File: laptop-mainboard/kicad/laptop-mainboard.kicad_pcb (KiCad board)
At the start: 8 copper layers, 330 x 115 mm, 112 parts, among them Q1 SiSS22DN, Q2 SiSS22DN, Q3 SiSS22DN, Q4 SiSS22DN, Q5 BATFET, U1 TPS65988 PD, U11 MP2857, U12 Stage CPU1, U13 Stage CPU2, U14 Stage CPU3, U15 Stage CPU4, U16 Stage SOC1, U17 Stage SOC2, U18 1V1_MEM, U19 W25Q256JW, U2 PD-Cfg, U21 SSD1-SW, U22 SSD2-SW, U23 JHL8540 TB4, U28 HD3SS3220, U29 HD3SS3220, U3 BQ25731, U30 VBUS-SW, U31 VBUS-SW, U32 VBUS-SW, U33 VBUS-SW, U34 RTL8125BG, U35 RTL8125BG, U36 TPD12S016, U37 VLCD-SW, U38 MP3389 BL, U39 ALC256, U4 5V Buck, U40 GL3224 SD, U41 IT5570E EC, U42 EC-Flash, U5 3V3 Buck, U6 1V8, U7 1V05_TB, U8 0V88_TB, U9 3V3_ALW, Y1 32.768k, Y3 25M, Y4 25M

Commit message: Rev B: echte AM5-Pinbelegung, Kleinteile, EliteBook-850-G7-Format
- AM5-Pinmap (1718 Pins, WikiChip/Wikimedia Public Domain) als CSV,
  Sockel-Footprint mit echten Padnamen und 1708 Signal-Netzen im Board
- Blatt 10: MLCC-Baenke, 11 ESD-Arrays, USB2-Chokes, Straps; 48-MHz-Quarz;
  beidseitige Bestueckung (B.Cu) mit Kollisionspruefung pro Seite
- Board 340x112mm im EliteBook-850-G7-Layout: USB-C-100W-PD an der
  Barrel-Jack-Position, TB4/HDMI/USB-A/RJ45 rechts, USB-A/Klinke links,
  HP-Akku 3S/56Wh, HP-FPC-Steckplaetze (Pinouts zu verifizieren)
- GND-Stitching-Vias, MDI-/DP-Korridore, 645 Board-Netze
- Renderer tools/render_board.py erzeugt docs/board_render.png
- Doku: elitebook.md neu, grenzen.md/README/power/layout aktualisiert

Co-Authored-By: Claude Fable 5 <noreply@anthropic.com>
Claude-Session: https://claude.ai/code/session_01E8mU1RUAv938Hs69waADCc
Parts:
- removed C14: 1n/2kV, laptop_mainboard:C_1812
- removed the C5 at (104.0, 122.0)
- removed J_LAN2: 2.5GbE, laptop_mainboard:RJ45_MAGJACK
- removed J_SD: SD UHS-II, laptop_mainboard:SD_PUSH
- removed J_USBC2, J_USBC3: USB-C 10G, laptop_mainboard:USBC_24
- removed U28, U29: HD3SS3220, laptop_mainboard:QFN30_4x4
- removed U30, U31: VBUS-SW, laptop_mainboard:SOT23-5
- removed U35: RTL8125BG, laptop_mainboard:QFN48_6x6
- removed U40: GL3224 SD, laptop_mainboard:QFN48_6x6
- removed Y4: 25M, laptop_mainboard:XTAL_3225
- added C20: 22u, laptop_mainboard:R_0603, B.Cu at (112.0, 72.0)
- added C21: 22u, laptop_mainboard:R_0603, B.Cu at (122.0, 72.0)
- added C22: 22u, laptop_mainboard:R_0603, B.Cu at (132.0, 72.0)
- added C23: 22u, laptop_mainboard:R_0603, B.Cu at (142.0, 72.0)
- added C24: 22u, laptop_mainboard:R_0603, B.Cu at (112.0, 80.0)
- added C25: 22u, laptop_mainboard:R_0603, B.Cu at (122.0, 80.0)
- added C26: 22u, laptop_mainboard:R_0603, B.Cu at (132.0, 80.0)
- added C27: 22u, laptop_mainboard:R_0603, B.Cu at (142.0, 80.0)
- added C28: 22u, laptop_mainboard:R_0603, B.Cu at (112.0, 88.0)
- added C29: 22u, laptop_mainboard:R_0603, B.Cu at (122.0, 88.0)
- added C30: 22u, laptop_mainboard:R_0603, B.Cu at (132.0, 88.0)
- added C31: 22u, laptop_mainboard:R_0603, B.Cu at (142.0, 88.0)
- added C32: 22u, laptop_mainboard:R_0603, B.Cu at (104.0, 96.0)
- added C33: 22u, laptop_mainboard:R_0603, B.Cu at (114.0, 96.0)
- added C34: 22u, laptop_mainboard:R_0603, B.Cu at (124.0, 96.0)
- added C35: 22u, laptop_mainboard:R_0603, B.Cu at (104.0, 64.0)
- added C36: 22u, laptop_mainboard:R_0603, B.Cu at (114.0, 64.0)
- added C40: 10u, laptop_mainboard:R_0603, B.Cu at (170.0, 60.0)
- added C41: 10u, laptop_mainboard:R_0603, B.Cu at (178.0, 60.0)
- added C42: 10u, laptop_mainboard:R_0603, B.Cu at (186.0, 60.0)
- added C43: 10u, laptop_mainboard:R_0603, B.Cu at (194.0, 60.0)
- added C44: 10u, laptop_mainboard:R_0603, B.Cu at (202.0, 60.0)
- added C45: 10u, laptop_mainboard:R_0603, B.Cu at (210.0, 60.0)
- added C46: 10u, laptop_mainboard:R_0603, B.Cu at (218.0, 60.0)
- added C47: 10u, laptop_mainboard:R_0603, B.Cu at (226.0, 60.0)
- added C48: 10u, laptop_mainboard:R_0603, B.Cu at (234.0, 60.0)
- added C49: 10u, laptop_mainboard:R_0603, B.Cu at (242.0, 60.0)
- added C52: 100n, laptop_mainboard:R_0603, B.Cu at (170.0, 68.0)
- added C53: 100n, laptop_mainboard:R_0603, B.Cu at (178.0, 68.0)
- added C54: 100n, laptop_mainboard:R_0603, B.Cu at (186.0, 68.0)
- added C55: 100n, laptop_mainboard:R_0603, B.Cu at (194.0, 68.0)
- added C56: 100n, laptop_mainboard:R_0603, B.Cu at (202.0, 68.0)
- added C57: 100n, laptop_mainboard:R_0603, B.Cu at (210.0, 68.0)
- added C58: 100n, laptop_mainboard:R_0603, B.Cu at (218.0, 68.0)
- added C59: 100n, laptop_mainboard:R_0603, B.Cu at (226.0, 68.0)
- added C60: 100n, laptop_mainboard:R_0603, B.Cu at (234.0, 68.0)
- added C61: 100n, laptop_mainboard:R_0603, B.Cu at (242.0, 68.0)
- added FL1: CMC Webcam, laptop_mainboard:R_0603, B.Cu at (203.0, 40.0)
- added FL2: CMC WLAN, laptop_mainboard:R_0603, B.Cu at (292.0, 52.0)
- added H6: , laptop_mainboard:MTG_M2_5, F.Cu at (274.0, 80.0)
- added R10: 10k, laptop_mainboard:R_0603, B.Cu at (60.0, 40.0)
- added R11: 10k, laptop_mainboard:R_0603, B.Cu at (60.0, 46.0)
- added R12: 10k, laptop_mainboard:R_0603, B.Cu at (60.0, 52.0)
- added R13: 10k, laptop_mainboard:R_0603, B.Cu at (60.0, 58.0)
- added R14: 10k, laptop_mainboard:R_0603, B.Cu at (60.0, 64.0)
- added R15: 10k, laptop_mainboard:R_0603, B.Cu at (60.0, 70.0)
- added U5: 3V3 Buck, laptop_mainboard:QFN20_3x4, F.Cu at (109.0, 38.0)
- added U50: ESD TB0-L1, laptop_mainboard:DFN6_2x2, B.Cu at (344.0, 40.0)
- added U51: ESD TB0-L2, laptop_mainboard:DFN6_2x2, B.Cu at (344.0, 46.0)
- added U52: ESD TB1-L1, laptop_mainboard:DFN6_2x2, B.Cu at (344.0, 52.0)
- added U53: ESD TB1-L2, laptop_mainboard:DFN6_2x2, B.Cu at (344.0, 58.0)
- added U54: ESD USBA1, laptop_mainboard:DFN6_2x2, B.Cu at (46.0, 60.0)
- added U55: ESD USBA2, laptop_mainboard:DFN6_2x2, B.Cu at (344.0, 90.0)
- added U56: ESD HDMI-1, laptop_mainboard:DFN6_2x2, B.Cu at (342.0, 70.0)
- added U57: ESD HDMI-2, laptop_mainboard:DFN6_2x2, B.Cu at (342.0, 76.0)
- added U58: ESD CC, laptop_mainboard:DFN6_2x2, B.Cu at (350.0, 34.0)
- added U59: ESD TB-USB2, laptop_mainboard:DFN6_2x2, B.Cu at (344.0, 64.0)
- added U60: ESD A-USB2, laptop_mainboard:DFN6_2x2, B.Cu at (46.0, 68.0)
- added Y2: 48M, laptop_mainboard:XTAL_3225, F.Cu at (183.0, 48.0)
- C37: renamed from H6; value (none) -> 22u; footprint laptop_mainboard:MTG_M2_5 -> laptop_mainboard:R_0603; moved to B.Cu
- C5: renamed from U5; value 3V3 Buck -> 470u; footprint laptop_mainboard:QFN20_3x4 -> laptop_mainboard:CAP_7343
- J_BAT: value Akku 4S -> HP-Akku 3S 56Wh
- J_KB: value Tastatur -> HP-Tastatur
- J_TB0: value TB4 / 100W PD -> USB-C PD 100W + TB4
- J_TP: value Touchpad -> HP-Clickpad
- moved J_LAN1 316.9 mm to (352.0, 112.0), turned to 270 degrees
- moved J_USBA2 314.8 mm to (352.0, 90.0), turned to 270 degrees
- moved C13 274.2 mm to (330.0, 104.0)
- moved U34 273.1 mm to (325.0, 112.0)
- moved U33 264.7 mm to (330.0, 92.0)
- moved Y3 256.6 mm to (316.0, 118.0)
- moved C37 150.9 mm to (124.0, 64.0)
- moved C5 82.2 mm to (104.0, 120.0)
- moved BT1 51.0 mm to (223.0, 133.0), turned to 90 degrees
- moved J_SPKR 39.3 mm to (276.0, 131.0)
- moved J_USBA1 36.0 mm to (40.0, 60.0)
- moved U32 33.5 mm to (58.0, 60.0)
- moved J_AUX 30.0 mm to (38.0, 84.0)
- moved J_HDMI 26.0 mm to (350.0, 70.0)
- moved H7 19.6 mm to (28.0, 105.0)
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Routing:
- net (no net): track 3613.1 -> 4365.7 mm
- net GND: vias 0 -> 83
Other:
- board size 330 x 115 mm -> 340 x 112 mm
- board text added: "HP-Akkuschacht (3S 56Wh) unterhalb"
- board text added: "Laptop-Mainboard fuer HP EliteBook 850 G7 - Rev B"
- board text added: "Umriss + Lochbild am realen 850-G7-Chassis verifizieren (docs/elitebook.md)"
- board text removed: "Akku-Bereich unterhalb der Platine"
- board text removed: "Korridore In1/In6: DDR5- und PCIe-Gen4-Paare (repraesentativ, Feinrouting offen)"
- board text removed: "Laptop-Mainboard 15.6" Rev A"

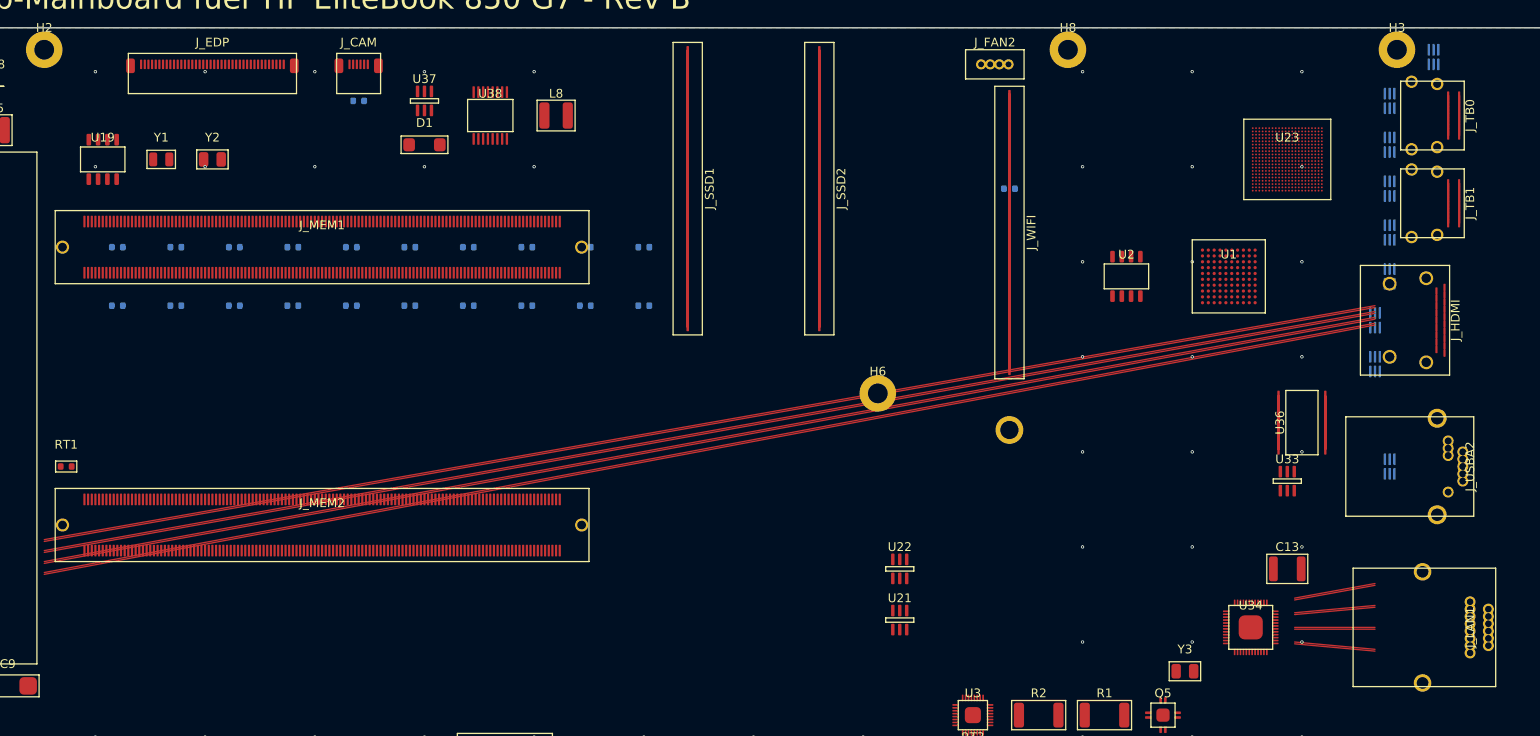
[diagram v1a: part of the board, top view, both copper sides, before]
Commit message: Portlayout nach Fotos des Originalgeraets korrigiert
- Rechte Kante hinten->vorn: USB-C-Ladeport 100W (Barrel-Position,
  eigener TPS65987D + Config-Flash, neues Blatt 07_ladeport), USB-A,
  HDMI, 2x USB-C Thunderbolt 4 nebeneinander (JHL8540)
- Kein RJ45 (Original hat keines): Ethernet entfernt, G0/G1 Reserve
- TPS65988 nur noch Source fuer die TB-Ports; breite VBUS_IN-Trasse
  vom Ladeport zum BQ25731
- Interne Anschlusspositionen des Original-Mainboards (Nutzerfoto)
  als Referenztabelle in docs/elitebook.md dokumentiert
- Doku, Blockdiagramm, BOM und Rendering aktualisiert

Co-Authored-By: Claude Fable 5 <noreply@anthropic.com>
Claude-Session: https://claude.ai/code/session_01E8mU1RUAv938Hs69waADCc
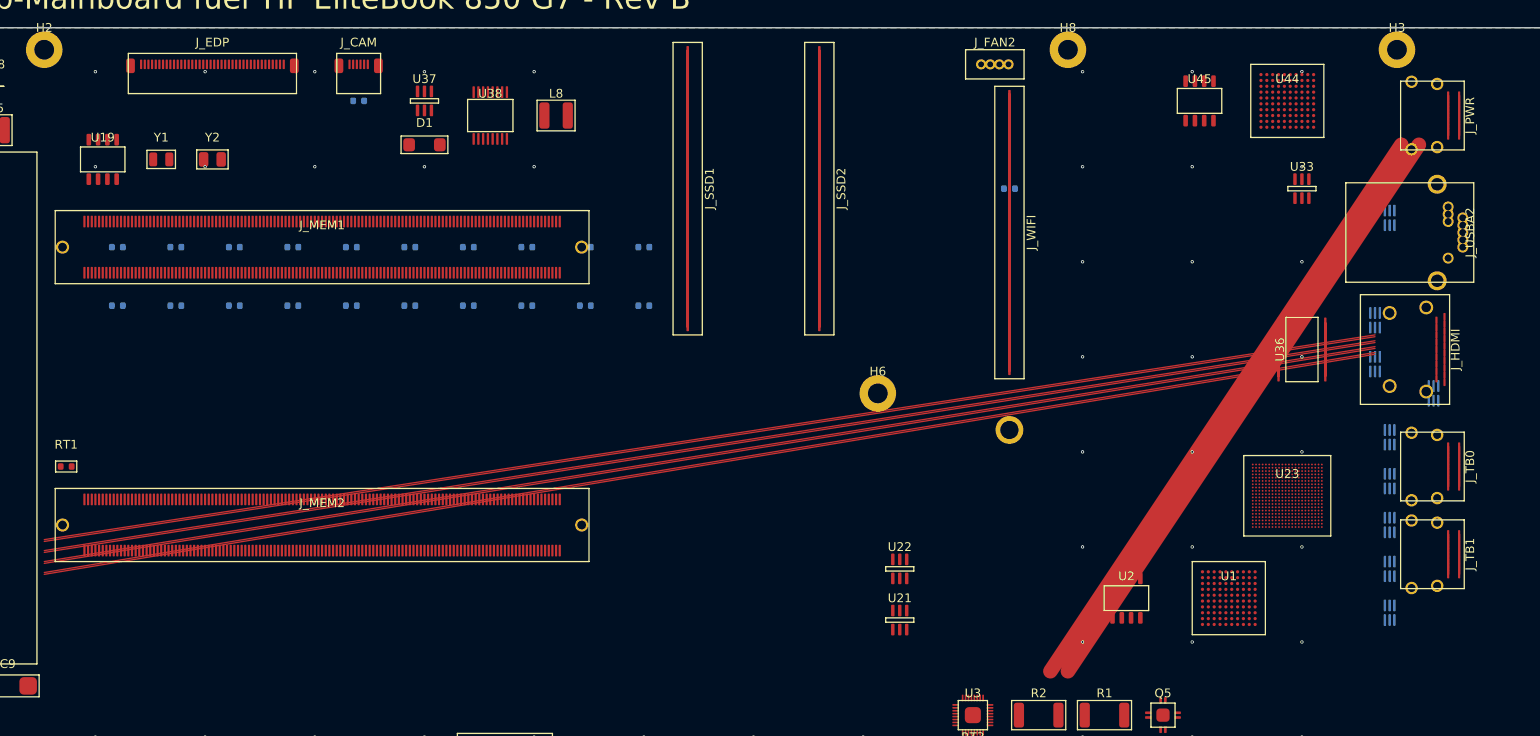
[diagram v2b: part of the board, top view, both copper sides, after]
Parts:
- removed C13: 1n/2kV, laptop_mainboard:C_1812
- removed the C20 at (112.0, 72.0)
- removed J_LAN1: 2.5GbE, laptop_mainboard:RJ45_MAGJACK
- removed the L10 at (109.0, 44.0)
- removed the U1 at (322.0, 64.0)
- removed U34: RTL8125BG, laptop_mainboard:QFN48_6x6
- removed the U6 at (129.0, 38.0)
- removed the U9 at (120.0, 38.0)
- removed Y3: 25M, laptop_mainboard:XTAL_3225
- added H1: , laptop_mainboard:MTG_M2_5, F.Cu at (28.0, 33.0)
- added J_PWR: USB-C Ladeport 100W, laptop_mainboard:USBC_24, F.Cu at (352.0, 42.0)
- added U36: TPD12S016, laptop_mainboard:TSSOP24, F.Cu at (332.0, 74.0)
- added U4: 5V Buck, laptop_mainboard:QFN20_3x4, F.Cu at (98.0, 38.0)
- added U44: TPS65987D Ladeport, laptop_mainboard:BGA96_9x9, F.Cu at (330.0, 40.0)
- added U45: PD2-Cfg, laptop_mainboard:SOIC8, F.Cu at (318.0, 40.0)
- added U5: 3V3 Buck, laptop_mainboard:QFN20_3x4, F.Cu at (109.0, 38.0)
- added U7: 1V05_TB, laptop_mainboard:DFN6_2x2, F.Cu at (137.0, 38.0)
- C20: renamed from H8; value (none) -> 22u; footprint laptop_mainboard:MTG_M2_5 -> laptop_mainboard:R_0603; moved to B.Cu
- J_TB0: value USB-C PD 100W + TB4 -> USB-C TB4
- J_TB1: value TB4 -> USB-C TB4
- L10: renamed from U7; value 1V05_TB -> 1u; footprint laptop_mainboard:DFN6_2x2 -> laptop_mainboard:IND_4x4
- U1: renamed from U36; value TPD12S016 -> TPS65988 PD; footprint laptop_mainboard:TSSOP24 -> laptop_mainboard:BGA96_9x9
- U6: renamed from U5; value 3V3 Buck -> 1V8; footprint laptop_mainboard:QFN20_3x4 -> laptop_mainboard:DFN6_2x2
- U9: renamed from U4; value 5V Buck -> 3V3_ALW
- moved H4 332.0 mm to (30.0, 138.0)
- moved H8 281.4 mm to (300.0, 33.0)
- moved H7 247.3 mm to (28.0, 105.0)
- moved H5 210.0 mm to (240.0, 139.0)
- moved C20 192.0 mm to (112.0, 72.0)
- moved H3 185.0 mm to (345.0, 33.0)
- moved H2 132.0 mm to (160.0, 33.0)
- moved U58 76.2 mm to (344.0, 110.0)
- moved H6 68.1 mm to (274.0, 80.0)
- moved J_TB0 48.0 mm to (352.0, 90.0)
- moved J_TB1 48.0 mm to (352.0, 102.0)
- moved U23 46.0 mm to (330.0, 94.0)
- moved U50 46.0 mm to (344.0, 86.0)
- moved U51 46.0 mm to (344.0, 92.0)
- moved U52 46.0 mm to (344.0, 98.0)
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- renumbered H1 to H2, H2 to H3, H3 to H4, H4 to H5, H5 to H6, H6 to H7, H7 to H8
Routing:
- net (no net): track 4365.7 -> 4470.8 mm
